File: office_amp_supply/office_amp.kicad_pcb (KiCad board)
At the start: 2 copper layers, 160 x 100 mm, 51 parts, among them J1 Jack-DC, J2 Conn_01x09_Socket, Q1 DMT6012LSS, U1 LM74700, U2 LM2576HVT-ADJ, U3 LM7805_TO220, U4 TBA_2-2421, U5 VXO78012_TO220

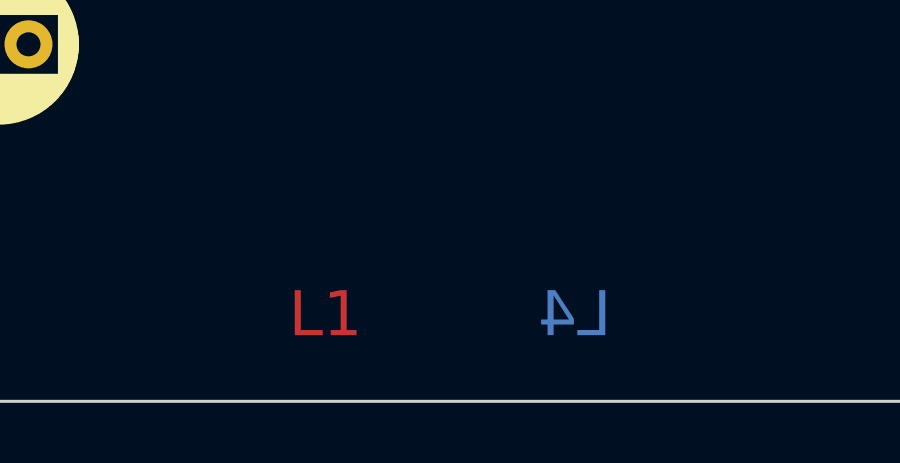
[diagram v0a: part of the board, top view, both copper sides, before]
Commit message: first positioning office-amp
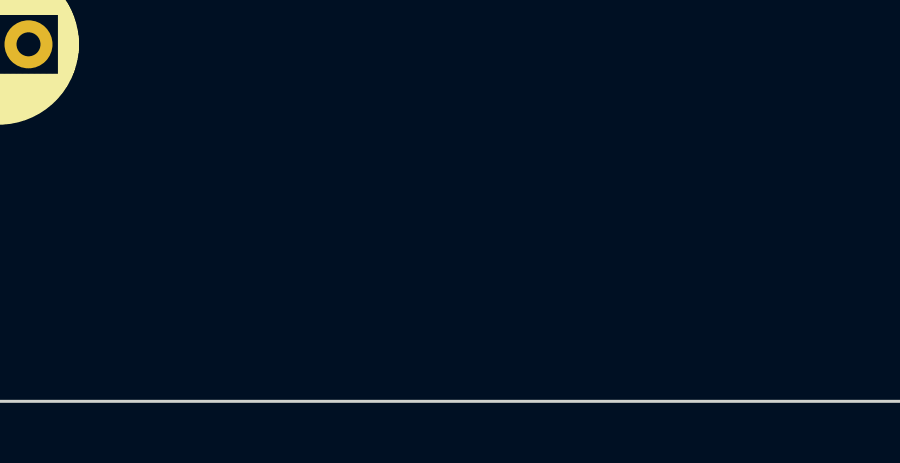
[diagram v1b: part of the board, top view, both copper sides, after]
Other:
- board text removed: "L1"
- board text removed: "L4"
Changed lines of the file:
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@@
   (paper "A4")
   (title_block
-    (comment 4 "AISLER Project ID: ZXJCEKVF")
+    (title "Office Amp Supply Prototype")
+    (date "2023-07-20")
+    (rev "V1.3")
   )
   (layers
@@
   (gr_line (start 90 158) (end 90 58)
     (stroke (width 0.1) (type solid)) (layer "Edge.Cuts"))
-  (gr_text "L1" (at 179.9 155.1) (layer "F.Cu")
-    (effects (font (size 1.5 1.5) (thickness 0.3)))
-  )
-  (gr_text "L4" (at 188.2 155.1) (layer "B.Cu")
-    (effects (font (size 1.5 1.5) (thickness 0.3)) (justify mirror))
-  )
   (gr_text "42Volt.de" (at 235.3 152.6) (layer "B.SilkS")
     (effects (font (size 0.8 0.8) (thickness 0.15)) (justify mirror))
@@
       )
     )
-  )
-  (zone (net 0) (net_name "") (layers "F&B.Cu") (hatch edge 0.508)
-    (connect_pads (clearance 0))
-    (min_thickness 0.254) (filled_areas_thickness no)
-    (keepout (tracks not_allowed) (vias not_allowed) (pads not_allowed) (copperpour not_allowed) (footprints allowed))
-    (fill (thermal_gap 0.508) (thermal_bridge_width 0.508))
-    (polygon
-      (pts
-        (xy 190.5 157)
-        (xy 177.8 157)
-        (xy 177.8 152.7)
-        (xy 190.5 152.7)
-      )
-    )

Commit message: first prototype supply
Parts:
- removed REF**: MountingHole_3.5mm_Pad, MountingHole:MountingHole_3.5mm_Pad
- removed STAR1: SolderJumper_2_Bridged, Jumper:SolderJumper-2_P1.3mm_Bridged_RoundedPad1.0x1.5mm
- C10, C15, C16, R5, R6, R7: moved to B.Cu
- C12, C13, C6: moved to F.Cu
- J2: footprint Connector_Dsub:DSUB-9_Female_Horizontal_P2.77x2.84mm_EdgePinOffset4.94mm_Housed_MountingHolesOffset7.48mm -> Connector_Dsub:DSUB-9_Male_Horizontal_P2.77x2.84mm_EdgePinOffset4.94mm_Housed_MountingHolesOffset7.48mm
- moved J2 125.4 mm to (138.6, 150.2)
- moved C7 121.3 mm to (103.0, 126.0)
- moved TP7 103.0 mm to (128.0, 136.0)
- moved C2 90.8 mm to (189.0, 68.0), turned to 180 degrees
- moved C8 89.3 mm to (134.0, 88.0), turned to 0 degrees
- moved TP5 85.2 mm to (123.0, 145.0)
- moved L2 83.4 mm to (155.7, 65.9), turned to 180 degrees
- moved C11 74.4 mm to (150.0, 73.9), turned to 180 degrees
- moved U4 68.8 mm to (113.0, 125.8)
- moved R2 66.9 mm to (190.0, 86.0), turned to -90 degrees
- moved R1 66.0 mm to (190.0, 82.0), turned to -90 degrees
- moved TP6 64.9 mm to (123.0, 127.3)
- moved C12 63.9 mm to (118.0, 141.0)
- moved C5 62.1 mm to (181.0, 108.0), turned to 0 degrees
- moved C13 61.1 mm to (118.0, 133.0)
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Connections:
- C1 pad 2: GNDREF -> GNDD
- C10 pad 2: GNDREF -> GNDD
- C11 pad 2: GNDREF -> GNDD
- C14 pad 2: GNDREF -> GNDD
- C17 pad 2: GNDREF -> GNDD
- C2 pad 2: GNDREF -> GNDD
- C4 pad 2: GNDREF -> GNDD
- C5 pad 1: -5V -> GNDD
- C5 pad 2: GNDREF -> -5V
- C6 pad 1: -5V -> GNDD
- C6 pad 2: GNDREF -> -5V
- C8 pad 2: GNDREF -> GNDD
- C9 pad 2: GNDREF -> GNDD
- J1 pad 2: GNDREF -> GNDD
- J2 pad 1: GNDREF -> -5V
- J2 pad 2: V+ -> +5V
- J2 pad 4: +5V -> GNDD
- J2 pad 5: -5V -> V+
- J2 pad 9: unconnected-(J2-Pin_9-Pad9) -> GNDD
- L1 pad 2: GNDREF -> GNDD
- R1 pad 1: GNDREF -> GNDD
- R4 pad 2: GNDREF -> GNDD
- TP2 pad 1: GNDREF -> GNDD
- U1 pad 2: GNDREF -> GNDD
- U3 pad 2: GNDREF -> GNDD
- U5 pad 2: GNDREF -> GNDD
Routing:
- net GNDD: track 0.00 -> 520.4 mm, vias 0 -> 2
- net V+: track 0.00 -> 305.1 mm, vias 0 -> 6
- net -5V: track 0.00 -> 147.0 mm, vias 0 -> 1
- net +12V: track 0.00 -> 94.0 mm, vias 0 -> 4
- net /Vin: track 0.00 -> 60.2 mm, vias 0 -> 1
- net +5V: track 0.00 -> 56.7 mm, vias 0 -> 2
- net Net-(C11-Pad1): track 0.00 -> 43.0 mm
- net GND_Input: track 0.00 -> 42.3 mm
- net -5VA: track 0.00 -> 42.0 mm, vias 0 -> 1
- net +5VA: track 0.00 -> 35.0 mm, vias 0 -> 1
- net Net-(D1-K): track 0.00 -> 19.9 mm
- net Net-(U5-VI): track 0.00 -> 16.2 mm
- net Net-(U4--VIN): track 0.00 -> 13.2 mm
- net Net-(U4-+VIN): track 0.00 -> 13.1 mm
- net Net-(U4-Common): track 0.00 -> 11.0 mm
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- added copper zone on B.Cu, net GNDD
- added copper zone on F.Cu, net GNDD
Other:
- board size 160 x 100 mm -> 117.1 x 100 mm
- board text added: "+12V"
- board text added: "+5VA"
- board text added: "-5V"
- board text added: "-5VA"
- board text added: "CW-AMP Supply V1.3"
- board text added: "GNDREF"
- board text added: "GND_Input"
- board text added: "V+"
- board text removed: "42Volt.de"
- board text removed: "Analog-IN ext. Analog-IN int."
- board text removed: "CW-AMP V1.3 Lars Nienhaus Tim Leininger Josef Borgert"
- board text removed: "L+"
- board text removed: "L-"
- board text removed: "R+"
- board text removed: "R-"
- board text removed: "www.campuswoche.de"
